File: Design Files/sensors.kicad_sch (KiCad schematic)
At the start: 12 parts, among them U15 AK09918C, U19 ICM-20602, U20 MMC5983MA, U25 BMP390

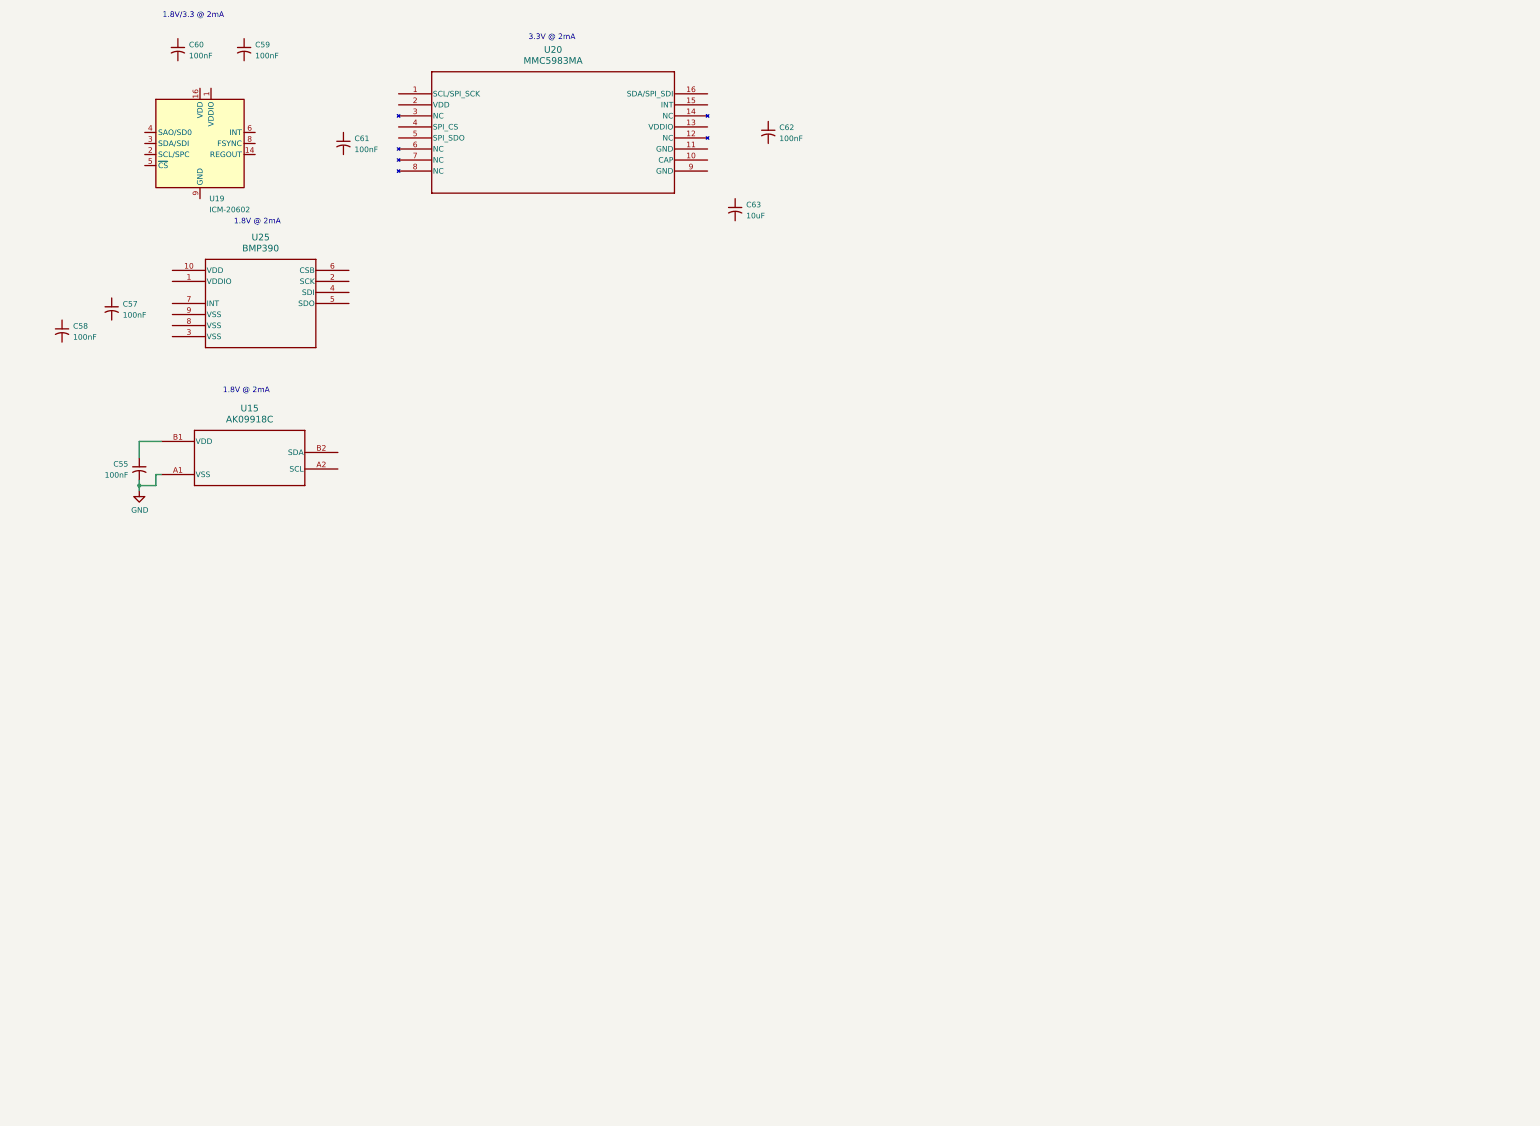
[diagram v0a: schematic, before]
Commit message: Prelim work on autopilot sensors complete
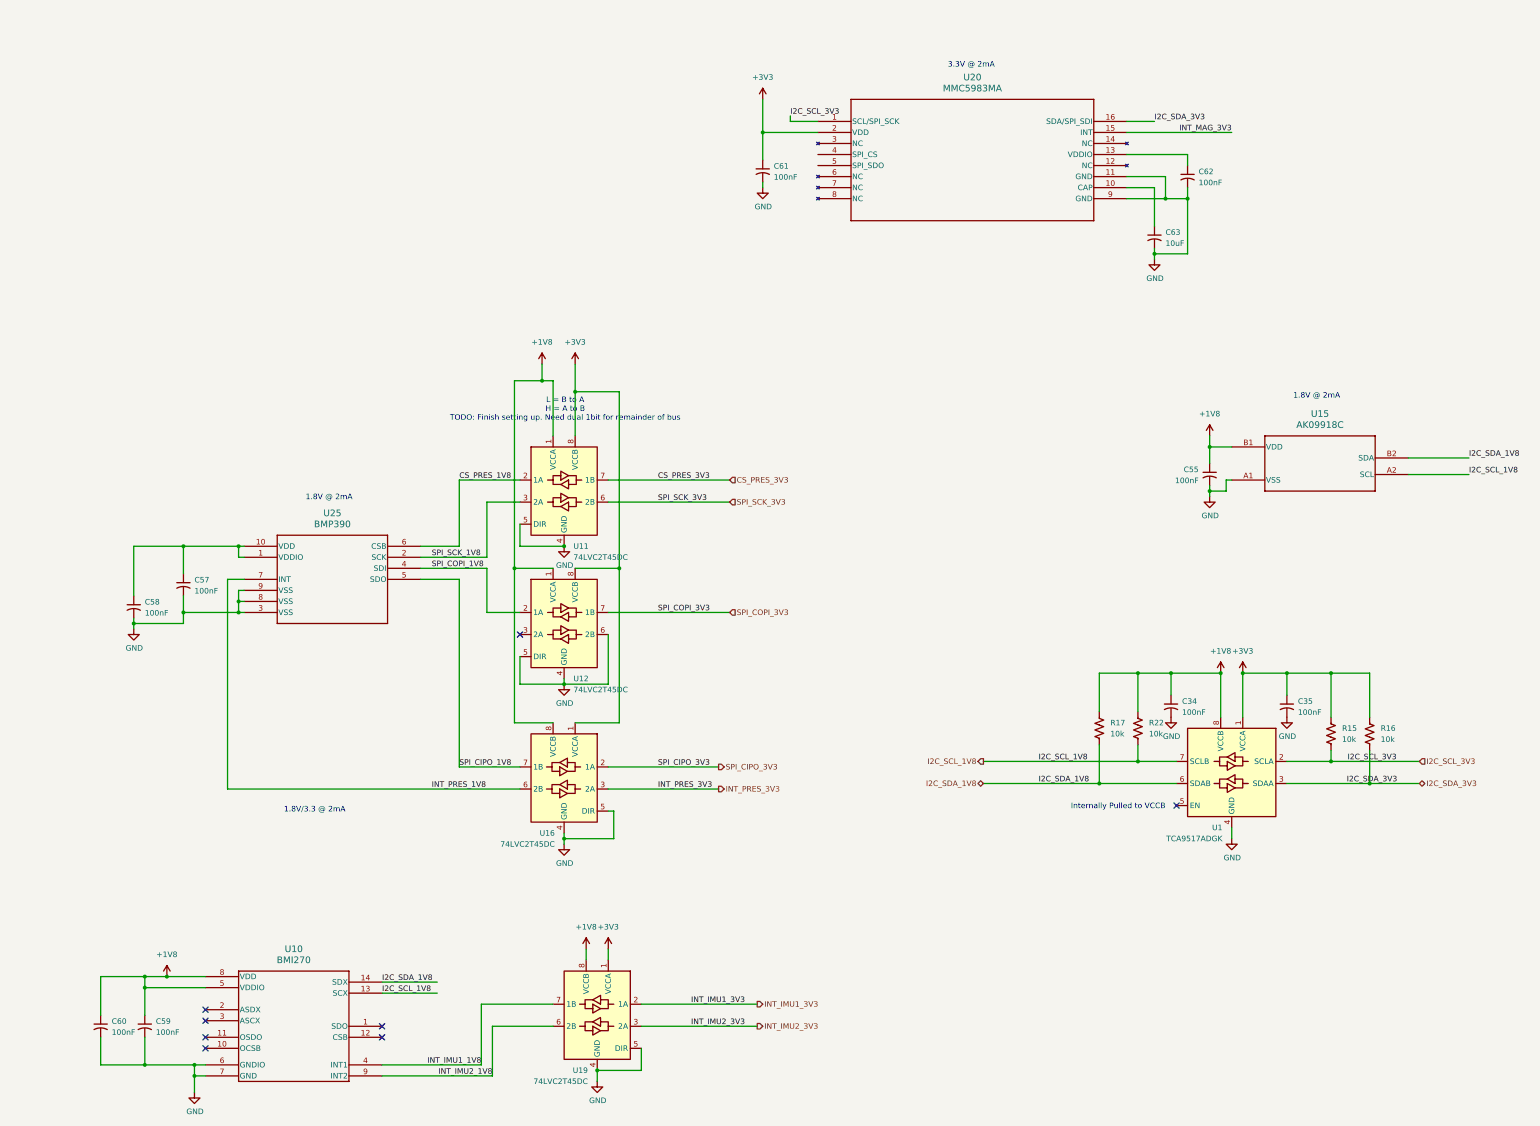
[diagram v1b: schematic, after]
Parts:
- removed U19: ICM-20602, Package_LGA:LGA-16_3x3mm_P0.5mm_LayoutBorder3x5y, symbol Sensor_Motion:ICM-20602
- added C34, C35: 100nF, Capacitor_SMD:C_0402_1005Metric, symbol Device:C_Small_US
- added R15, R16, R17, R22: 10k, Resistor_SMD:R_0402_1005Metric_Pad0.72x0.64mm_HandSolder, symbol Device:R_US
- added U1: TCA9517ADGK, Package_SO:VSSOP-8_3x3mm_P0.65mm, symbol Logic_LevelTranslator:TCA9517ADGK
- added U10: BMI270, SiGe_Lib:BMI270_BOS, symbol SiGe_Lib:BMI270
- added U11, U12, U16, U19: 74LVC2T45DC, Package_SO:VSSOP-8_2.3x2mm_P0.5mm, symbol Logic_LevelTranslator:74LVC2T45DC
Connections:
- net GND: now also C57.2, C58.2, C59.2, C60.2, C61.2, C62.2, C63.2, U20.11 (GND), U20.9 (GND), U25.3 (VSS), U25.8 (VSS), U25.9 (VSS), C34.2, C35.2, U1.4 (GND), U10.6 (GNDIO), U10.7 (GND), U11.4 (GND), U11.5 (DIR), U12.4 (GND), U12.5 (DIR), U12.6 (2B), U16.4 (GND), U16.5 (DIR), U19.4 (GND), U19.5 (DIR)
- net at U25.1 (VDDIO): now also C57.1, C58.1, U25.10 (VDD)
- net SPI_SCK_1V8: now reaches U25.2 (SCK)
- net SPI_SCK_1V8: now also U11.3 (2A)
- net SPI_COPI_1V8: now reaches U25.4 (SDI)
- net SPI_COPI_1V8: now also U12.2 (1A)
- net SPI_CIPO_1V8: now reaches U25.5 (SDO)
- net SPI_CIPO_1V8: now also U16.7 (1B)
- net CS_PRES_1V8: now reaches U25.6 (CSB)
- net CS_PRES_1V8: now also U11.2 (1A)
- net INT_PRES_1V8: now reaches U25.7 (INT)
- net INT_PRES_1V8: now also U16.6 (2B)
- net I2C_SCL_1V8: now reaches U15.A2 (SCL)
- net I2C_SCL_1V8: now also R22.2, U1.7 (SCLB), U10.13 (SCX)
- net +1V8: now reaches C55.1, U15.B1 (VDD)
- net +1V8: now also C59.1, C60.1, C34.1, R17.1, R22.1, U1.8 (VCCB), U10.5 (VDDIO), U10.8 (VDD), U11.1 (VCCA), U12.1 (VCCA), U16.8 (VCCB), U19.8 (VCCB)
- net I2C_SDA_1V8: now reaches U15.B2 (SDA)
- net I2C_SDA_1V8: now also R17.2, U1.6 (SDAB), U10.14 (SDX)
- net +3V3: now reaches C61.1
- net +3V3: now also U20.2 (VDD), C35.1, R15.1, R16.1, U1.1 (VCCA), U11.8 (VCCB), U12.8 (VCCB), U16.1 (VCCA), U19.1 (VCCA)
- net I2C_SCL_3V3: now reaches U20.1 (SCL/SPI_SCK)
- net I2C_SCL_3V3: now also R15.2, U1.2 (SCLA)
- net at U20.10 (CAP): now also C63.1
- net at U20.13 (VDDIO): now also C62.1
- net INT_MAG_3V3: now reaches U20.15 (INT)
- net I2C_SDA_3V3: now reaches U20.16 (SDA/SPI_SDI)
- net I2C_SDA_3V3: now also R16.2, U1.3 (SDAA)
- new net CS_PRES_3V3: U11.7 (1B)
- new net INT_IMU1_1V8: U10.4 (INT1), U19.7 (1B)
- new net INT_IMU1_3V3: U19.2 (1A)
- new net INT_IMU2_1V8: U10.9 (INT2), U19.6 (2B)
- new net INT_IMU2_3V3: U19.3 (2A)
- new net INT_PRES_3V3: U16.3 (2A)
- new net SPI_CIPO_3V3: U16.2 (1A)
- new net SPI_COPI_3V3: U12.7 (1B)
- new net SPI_SCK_3V3: U11.6 (2B)
- no-connect marks 0 -> 8
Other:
- note added: "Internally Pulled to VCCB"
- note added: "L = B to A H = A to B TODO: Finish setting up. Need dual 1bit for remainder of bus"
- moved on the sheet: C55, C57, C58, C59, C60, C61, C62, C63, U15, U20, U25

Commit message: Fixed reversed I2C tranlator
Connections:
- net +1V8: now also U1.1 (VCCA); no longer U1.8 (VCCB)
- net +3V3: now also U1.8 (VCCB); no longer U1.1 (VCCA)
- net I2C_SCL_1V8: now also U1.2 (SCLA); no longer U1.7 (SCLB)
- net I2C_SCL_3V3: now also U1.7 (SCLB); no longer U1.2 (SCLA)
- net I2C_SDA_1V8: now also U1.3 (SDAA); no longer U1.6 (SDAB)
- net I2C_SDA_3V3: now also U1.6 (SDAB); no longer U1.3 (SDAA)

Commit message: Fixed power & GPIO nets
Added PWM I2C Bus
Replaced global power labels on the sensor page with hierarchical pins & page labels
Cleaned up CM5 GPIO block sheet
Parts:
- renumbered U1 to U24
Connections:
- net +1V8 is gone; now on net 1V8: C34.1, C55.1, C59.1, C60.1, R17.1, R22.1, U10.5 (VDDIO), U10.8 (VDD), U11.1 (VCCA), U12.1 (VCCA), U15.B1 (VDD), U16.8 (VCCB), U19.8 (VCCB), U24.1 (VCCA)
- net 1V8: now reaches C57.1, C58.1, U25.1 (VDDIO), U25.10 (VDD)
- net +3V3 renamed 3V3

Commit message: Additional layout updates
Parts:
- removed U19: 74LVC2T45DC, Package_SO:VSSOP-8_2.3x2mm_P0.5mm, symbol Logic_LevelTranslator:74LVC2T45DC
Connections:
- net MAG_VDDIO: now reaches C62.1, U20.13 (VDDIO)
- net INT_IMU1_1V8: no longer names the net of U10.4 (INT1)
- net INT_IMU2_1V8: no longer names the net of U10.9 (INT2)
- no-connect marks 8 -> 10
